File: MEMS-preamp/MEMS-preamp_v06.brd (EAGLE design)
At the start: 45.4 x 26.7 mm, 47 parts, among them Q1 OPA2134

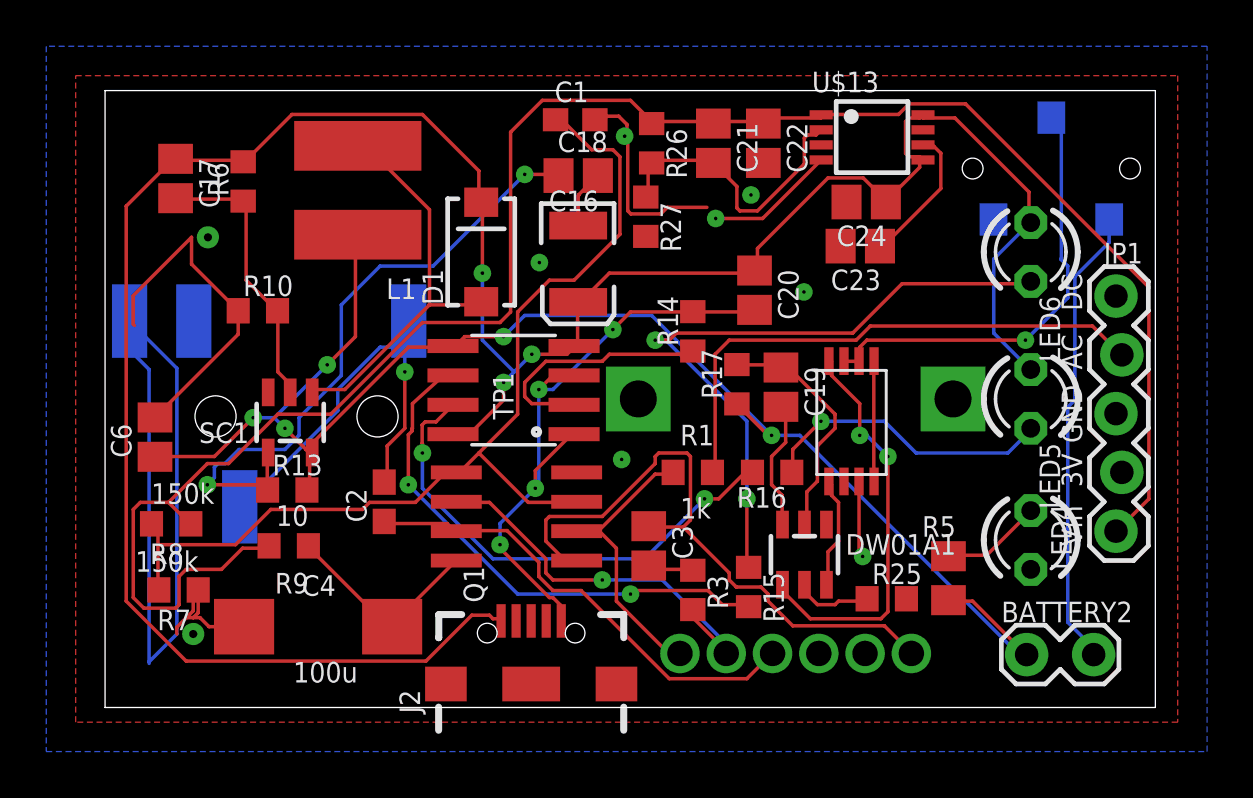
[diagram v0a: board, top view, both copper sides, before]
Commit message: mems power fixed
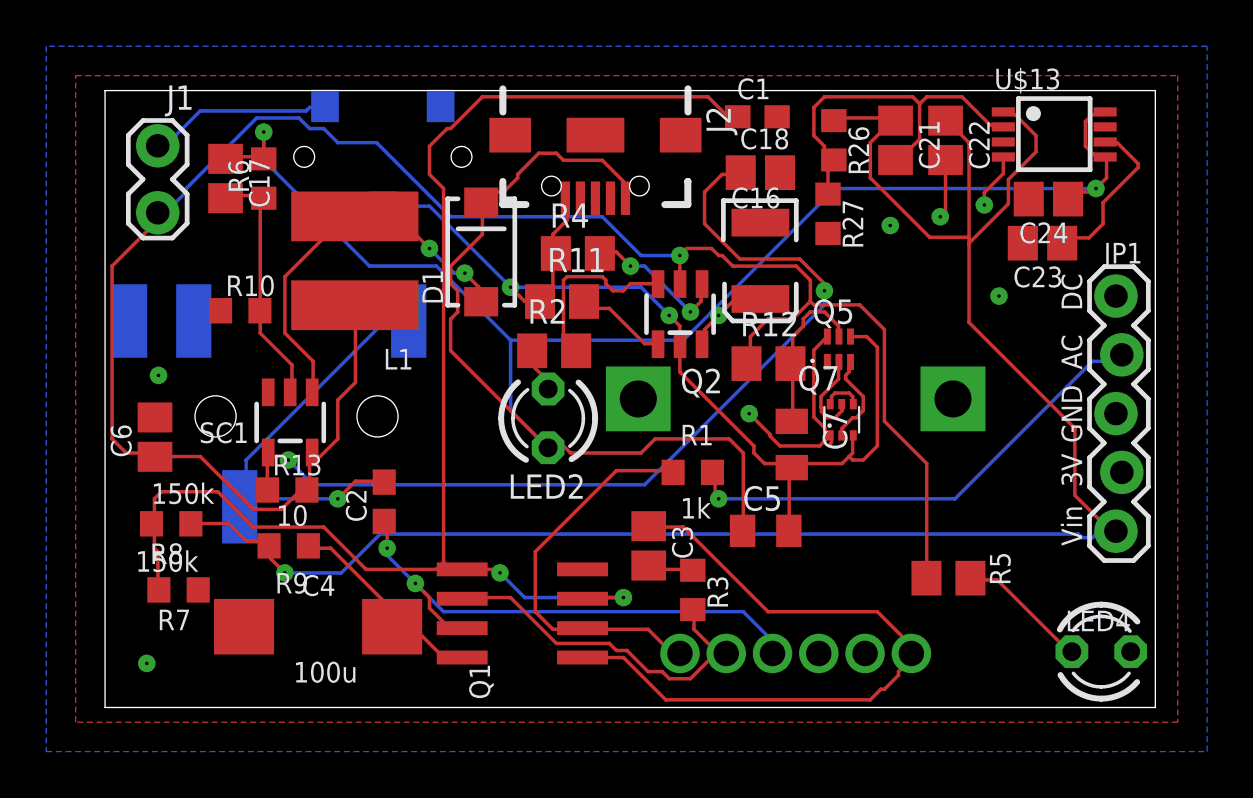
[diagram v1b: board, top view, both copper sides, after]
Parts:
- removed BATTERY2: (no value), SparkFun-Connectors:1X02_LOCK
- removed C19, C20: 0.1uF, adafruit:C0805
- removed DW01A1: DW01A, CMU-ArtFab:SOT23-6
- removed F8205A1: F8205A, CMU-ArtFab:F8205A
- removed LED5, LED6: (no value), led:LED3MM
- removed POWER1: SPDT, CMU-ArtFab:SWITCH_SPDT_CL-SB-12B
- removed R14: 1.2k, CMU-ArtFab:R0603
- removed R15, R16: 1k, CMU-ArtFab:R0603
- removed R17: nfo, CMU-ArtFab:R0603
- removed R25: 100, CMU-ArtFab:R0603
- removed TP1: TP4056-CHIP, CMU-ArtFab:SO08
- added C5: 10uF, adafruit:C0805K
- added C7: 0.1uF, adafruit:C0805K
- added J1: Battery, SparkFun-Connectors:1X02_LOCK
- added LED2: (no value), led:LED3MM
- added Q2: BQ21040, CMU-ArtFab:SOT23-6
- added Q5: BQ297X, CMU-ArtFab:WSON-6
- added Q7: DMN2400, CMU-ArtFab:SOT-563
- added R11, R4: 10k, CMU-ArtFab:R0805
- added R12: 330, CMU-ArtFab:R0805
- added R2: 1k, CMU-ArtFab:R0805
- added SW1: SPDT, CMU-ArtFab:SWITCH_SPDT_CL-SB-12B
- moved J2 23.9 mm to (21.2, 24.1), turned to 270 degrees
- moved C16 7.88 mm to (28.3, 18.7)
- moved C18 7.88 mm to (28.3, 22.5)
- moved C22 7.88 mm to (36.3, 23.9)
- moved C24 7.88 mm to (40.8, 21.3)
- moved R27 7.88 mm to (31.2, 20.7)
- moved U$13 7.88 mm to (41.0, 24.1)
- moved C1 7.88 mm to (28.2, 24.9)
- moved R26 7.88 mm to (31.5, 23.9)
- moved C21 7.88 mm to (34.2, 23.9)
- moved C23 7.88 mm to (40.5, 19.4)
- moved LED4 5.71 mm to (43.1, 1.78), turned to 0 degrees
- moved Q1 4.20 mm to (18.0, 3.43)
- moved L1 3.05 mm to (10.8, 18.7)
- moved C17 2.16 mm to (5.21, 22.2)
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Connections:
- removed net N$23: LED5.K, R16.1
- removed net N$24: DW01A1.1, F8205A1.P$4
- removed net N$25: DW01A1.3, F8205A1.P$5
- removed net N$27: C19.1, DW01A1.5, R17.2
- removed net N$31: C19.2, DW01A1.6
- removed net N$45: DW01A1.2, R25.1
- removed net N$46: F8205A1.P$1, F8205A1.P$8
- new net GND2: C5.2, C7.2, J2.GND, Q2.5, Q5.4, Q7.3, R11.1, R4.1, SW1.P$2
- new net N$18: C7.1, Q5.5, R12.2
- new net N$20: Q5.2, Q7.5
- net GND: now also Q5.6, Q7.1; no longer F8205A1.P$6, F8205A1.P$7, R25.2
- net N$11: now also LED2.K, R2.1; no longer BATTERY2.2, POWER1.P$1
- net N$15: now also Q2.3, R2.2; no longer C20.2, J2.GND, R14.2, TP1.1, TP1.3
- net N$16: now also Q2.1, R4.2; no longer R14.1, TP1.2
- net N$17: now also Q2.4, R11.2; no longer R16.2, TP1.7
- net N$19: now also Q7.4, Q7.6; no longer R15.2, TP1.6
- net N$22: now also Q5.3, Q7.2; no longer LED6.K, R15.1
- net N$6: now also J1.2, SW1.P$1; no longer F8205A1.P$2, F8205A1.P$3, POWER1.P$2
- net V+: now also C5.1, LED2.A, Q2.6; no longer C20.1, LED5.A, LED6.A, TP1.4, TP1.8
- net VBAT: now also J1.1, Q2.2, R12.1; no longer BATTERY2.1, R17.1, TP1.5
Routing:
- net GND: track 72.8 -> 14.6 mm, vias 9 -> 7
- net GND2: track 0.00 -> 44.0 mm, vias 0 -> 2
- net N$22: track 29.1 -> 4.05 mm, vias 2 -> 0
- net N$19: track 22.8 -> 1.75 mm, vias 2 -> 0
- net VBAT: track 65.6 -> 85.3 mm, vias 5 -> 1
- net N$15: track 27.7 -> 7.95 mm, vias 4 -> 0
- net N$8: track 43.1 -> 61.3 mm, vias 0 -> 2
- net N$17: track 22.2 -> 4.02 mm, vias 2 -> 0
- net N$11: track 20.0 -> 1.93 mm
- net N$24: track 17.6 -> 0.00 mm, vias 2 -> 0
- net V+: track 109.3 -> 95.6 mm
- net N$23: track 13.0 -> 0.00 mm, vias 1 -> 0
- net N$13: track 27.7 -> 40.1 mm
- net N$6: track 19.2 -> 8.01 mm, vias 1 -> 0
- net N$27: track 10.5 -> 0.00 mm
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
